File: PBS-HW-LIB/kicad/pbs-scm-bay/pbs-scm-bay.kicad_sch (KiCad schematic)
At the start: 10 parts, among them J1 Module receptacle, blind-mate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, J2 Host harness connector, J3 Identity tag pigtail connecto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, J4 Coaxial host antenna port (SC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, SW1 Module-seated switch (signal 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, U1 ESD/TVS protection array (dat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

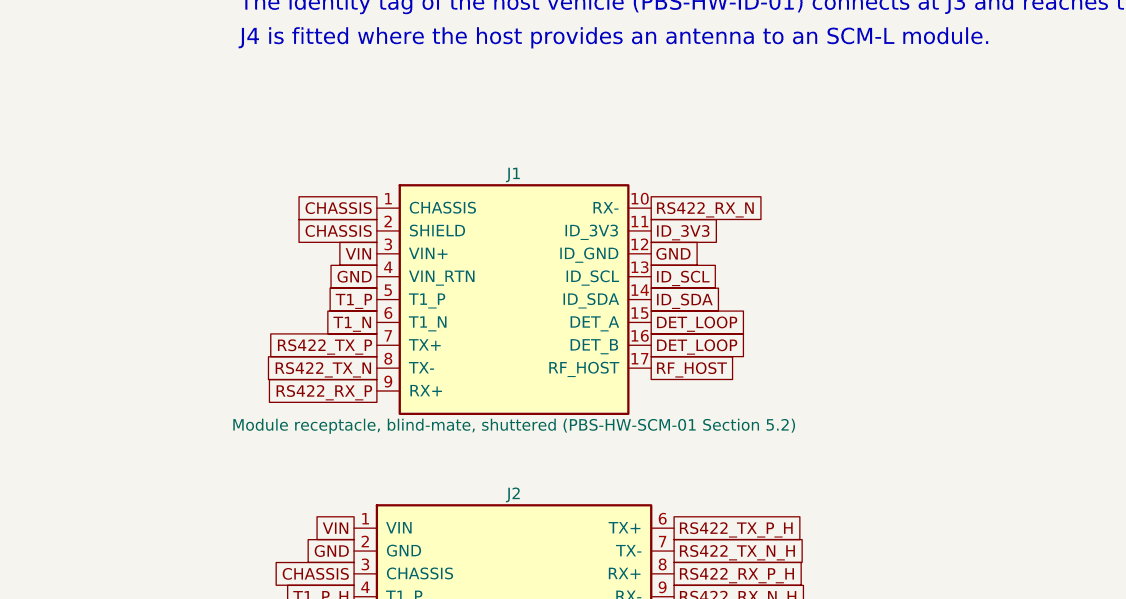
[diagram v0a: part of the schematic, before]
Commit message: Define the module host connector (PBS-HW-CON-01)
Add PBS-HW-CON-01: a face-to-face blind-mate connector with 17 contacts at
stated positions, flat pads on the module and spring contacts in the bay,
mating order set by four free heights 0.60 mm apart, keyed guide pins
(A 4.00, B 3.00), a bay cover plate and covered module apertures, an SMP
RF contact, forces and electrical ratings. Two dimensioned drawing sheets.

KiCad: both J1 footprints now follow the contact map (module half on the
back of the core board, centred; bay half with spring-contact holes and
guide pins), with 3D models showing contact heights, guide pins and the
cover plate. All geometry comes from tools/connector.py.

PBS-HW-SCM-01 v0.3 references the connector document.
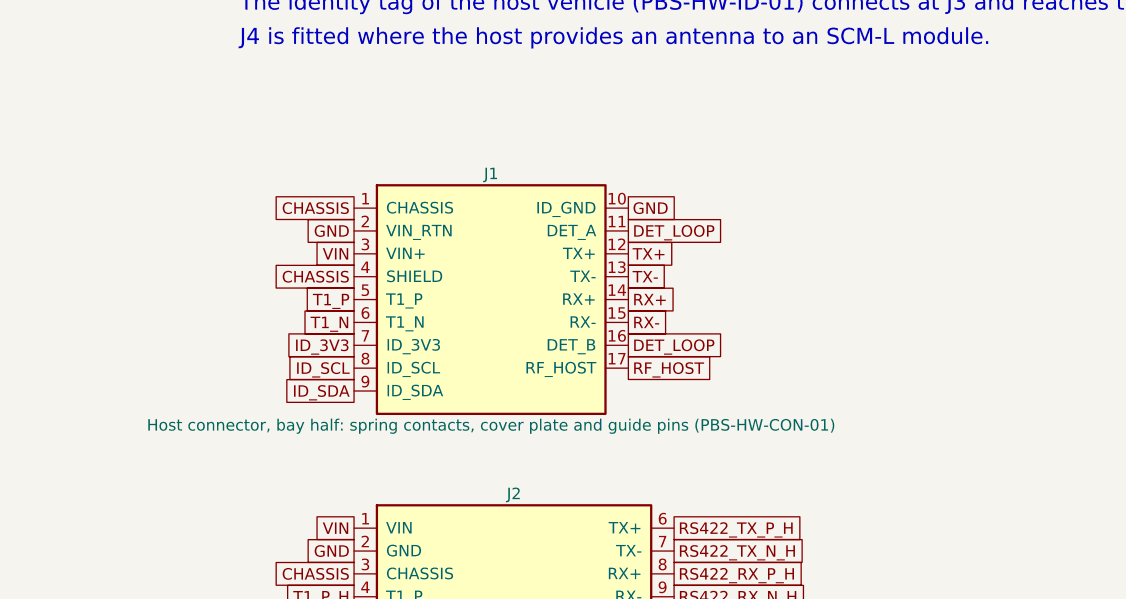
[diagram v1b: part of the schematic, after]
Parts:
- J1: value Module receptacle, blind-mate, shuttered (PBS-HW-SCM-01 Section 5.2) -> Host connector, bay half: spring contacts, cover plate and guide pins (PBS-HW-CON-01); footprint PBS_Generic:J1_Module_receptacle_blind_mate_shuttered_PBS_HW_SCM_01_Section_5_2 -> PBS_Generic:J1_Host_connector_bay_half_spring_contacts_cover_plate_and_guide_pins_PBS_HW_CON; symbol PBS_Generic:J1_Module_receptacle_blind_mate_shuttered_PBS_HW_SCM_01_Section_5_2 -> PBS_Generic:J1_Host_connector_bay_half_spring_contacts_cover_plate_and_guide_pins_PBS_HW_CON
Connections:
- net CHASSIS: now also J1.4 (SHIELD); no longer J1.2 (SHIELD)
- net DET_LOOP: now also J1.11 (DET_A); no longer J1.15 (DET_A)
- net GND: now also J1.10 (ID_GND), J1.2 (VIN_RTN); no longer J1.12 (ID_GND), J1.4 (VIN_RTN)
- net ID_3V3: now also J1.7 (ID_3V3); no longer J1.11 (ID_3V3)
- net ID_SCL: now also J1.8 (ID_SCL); no longer J1.13 (ID_SCL)
- net ID_SDA: now also J1.9 (ID_SDA); no longer J1.14 (ID_SDA)
- net RS422_RX_N: no longer J1.10 (RX-)
- net RS422_RX_P: no longer J1.9 (RX+)
- net RS422_TX_N: no longer J1.8 (TX-)
- net RS422_TX_P: no longer J1.7 (TX+)
- new net RX+: J1.14 (RX+)
- new net RX-: J1.15 (RX-)
- new net TX+: J1.12 (TX+)
- new net TX-: J1.13 (TX-)
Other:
- moved on the sheet: J1
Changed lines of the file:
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@@
 (kicad_sch (version 20231120) (generator "eeschema") (generator_version "8.0")
   (paper "A3")
-  (title_block (title "PBS-HW-SCM-01 host bay interface board: Bay interface") (date "2026-10-08") (rev "0.2") (company "Pale Blue Systems Foundation") (comment 1 "PBS-HW-SCM-01 open reference design; generic placeholders, no part numbers") (comment 2 "Generated by PBS-HW-LIB/kicad/tools/generate.py"))
-  (symbol (lib_id "PBS_Generic:J1_Module_receptacle_blind_mate_shuttered_PBS_HW_SCM_01_Section_5_2") (at 55.88 55.88 0) (unit 1) (exclude_from_sim no) (in_bom yes) (on_board yes) (dnp no)
-    (property "Reference" "J1" (at 55.88 41.91 0) (effects (font (size 1.27 1.27))))
-    (property "Value" "Module receptacle, blind-mate, shuttered (PBS-HW-SCM-01 Section 5.2)" (at 55.88 69.85 0) (effects (font (size 1.27 1.27))))
-    (property "Footprint" "PBS_Generic:J1_Module_receptacle_blind_mate_shuttered_PBS_HW_SCM_01_Section_5_2" (at 55.88 55.88 0) (effects (font (size 1.27 1.27)) hide))
-    (property "Datasheet" "" (at 55.88 55.88 0) (effects (font (size 1.27 1.27)) hide))
-    (property "Description" "Generic placeholder: Module receptacle, blind-mate, shuttered (PBS-HW-SCM-01 Section 5.2)" (at 55.88 55.88 0) (effects (font (size 1.27 1.27)) hide))
-    (property "Fit" "All" (at 55.88 72.39 0) (effects (font (size 1.27 1.27)) hide))
+  (title_block (title "PBS-HW-SCM-01 host bay interface board: Bay interface") (date "2026-10-08") (rev "0.3") (company "Pale Blue Systems Foundation") (comment 1 "PBS-HW-SCM-01 open reference design; generic placeholders, no part numbers") (comment 2 "Generated by PBS-HW-LIB/kicad/tools/generate.py"))
+  (symbol (lib_id "PBS_Generic:J1_Host_connector_bay_half_spring_contacts_cover_plate_and_guide_pins_PBS_HW_CON") (at 53.34 55.88 0) (unit 1) (exclude_from_sim no) (in_bom yes) (on_board yes) (dnp no)
+    (property "Reference" "J1" (at 53.34 41.91 0) (effects (font (size 1.27 1.27))))
+    (property "Value" "Host connector, bay half: spring contacts, cover plate and guide pins (PBS-HW-CON-01)" (at 53.34 69.85 0) (effects (font (size 1.27 1.27))))
+    (property "Footprint" "PBS_Generic:J1_Host_connector_bay_half_spring_contacts_cover_plate_and_guide_pins_PBS_HW_CON" (at 53.34 55.88 0) (effects (font (size 1.27 1.27)) hide))
+    (property "Datasheet" "" (at 53.34 55.88 0) (effects (font (size 1.27 1.27)) hide))
+    (property "Description" "Generic placeholder: Host connector, bay half: spring contacts, cover plate and guide pins (PBS-HW-CON-01)" (at 53.34 55.88 0) (effects (font (size 1.27 1.27)) hide))
+    (property "Fit" "All" (at 53.34 72.39 0) (effects (font (size 1.27 1.27)) hide))
     (pin "1")
     (pin "2")
@@
     (pin "17")
     (instances (project "pbs-scm-bay" (path "/f574994a-9591-5314-bf82-9cdc403f0860" (reference "J1") (unit 1)))))
-  (global_label "CHASSIS" (shape passive) (at 40.64 45.72 180) (fields_autoplaced yes) (effects (font (size 1.27 1.27)) (justify right)))
-  (global_label "CHASSIS" (shape passive) (at 40.64 48.26 180) (fields_autoplaced yes) (effects (font (size 1.27 1.27)) (justify right)))
-  (global_label "VIN" (shape passive) (at 40.64 50.8 180) (fields_autoplaced yes) (effects (font (size 1.27 1.27)) (justify right)))
-  (global_label "GND" (shape passive) (at 40.64 53.34 180) (fields_autoplaced yes) (effects (font (size 1.27 1.27)) (justify right)))
-  (global_label "T1_P" (shape passive) (at 40.64 55.88 180) (fields_autoplaced yes) (effects (font (size 1.27 1.27)) (justify right)))
-  (global_label "T1_N" (shape passive) (at 40.64 58.42 180) (fields_autoplaced yes) (effects (font (size 1.27 1.27)) (justify right)))
-  (global_label "RS422_TX_P" (shape passive) (at 40.64 60.96 180) (fields_autoplaced yes) (effects (font (size 1.27 1.27)) (justify right)))
-  (global_label "RS422_TX_N" (shape passive) (at 40.64 63.5 180) (fields_autoplaced yes) (effects (font (size 1.27 1.27)) (justify right)))
-  (global_label "RS422_RX_P" (shape passive) (at 40.64 66.04 180) (fields_autoplaced yes) (effects (font (size 1.27 1.27)) (justify right)))
-  (global_label "RS422_RX_N" (shape passive) (at 71.12 45.72 0) (fields_autoplaced yes) (effects (font (size 1.27 1.27)) (justify left)))
-  (global_label "ID_3V3" (shape passive) (at 71.12 48.26 0) (fields_autoplaced yes) (effects (font (size 1.27 1.27)) (justify left)))
-  (global_label "GND" (shape passive) (at 71.12 50.8 0) (fields_autoplaced yes) (effects (font (size 1.27 1.27)) (justify left)))
-  (global_label "ID_SCL" (shape passive) (at 71.12 53.34 0) (fields_autoplaced yes) (effects (font (size 1.27 1.27)) (justify left)))
-  (global_label "ID_SDA" (shape passive) (at 71.12 55.88 0) (fields_autoplaced yes) (effects (font (size 1.27 1.27)) (justify left)))
-  (global_label "DET_LOOP" (shape passive) (at 71.12 58.42 0) (fields_autoplaced yes) (effects (font (size 1.27 1.27)) (justify left)))
-  (global_label "DET_LOOP" (shape passive) (at 71.12 60.96 0) (fields_autoplaced yes) (effects (font (size 1.27 1.27)) (justify left)))
-  (global_label "RF_HOST" (shape passive) (at 71.12 63.5 0) (fields_autoplaced yes) (effects (font (size 1.27 1.27)) (justify left)))
+  (global_label "CHASSIS" (shape passive) (at 38.1 45.72 180) (fields_autoplaced yes) (effects (font (size 1.27 1.27)) (justify right)))
+  (global_label "GND" (shape passive) (at 38.1 48.26 180) (fields_autoplaced yes) (effects (font (size 1.27 1.27)) (justify right)))
+  (global_label "VIN" (shape passive) (at 38.1 50.8 180) (fields_autoplaced yes) (effects (font (size 1.27 1.27)) (justify right)))
+  (global_label "CHASSIS" (shape passive) (at 38.1 53.34 180) (fields_autoplaced yes) (effects (font (size 1.27 1.27)) (justify right)))
+  (global_label "T1_P" (shape passive) (at 38.1 55.88 180) (fields_autoplaced yes) (effects (font (size 1.27 1.27)) (justify right)))
+  (global_label "T1_N" (shape passive) (at 38.1 58.42 180) (fields_autoplaced yes) (effects (font (size 1.27 1.27)) (justify right)))
+  (global_label "ID_3V3" (shape passive) (at 38.1 60.96 180) (fields_autoplaced yes) (effects (font (size 1.27 1.27)) (justify right)))
+  (global_label "ID_SCL" (shape passive) (at 38.1 63.5 180) (fields_autoplaced yes) (effects (font (size 1.27 1.27)) (justify right)))
+  (global_label "ID_SDA" (shape passive) (at 38.1 66.04 180) (fields_autoplaced yes) (effects (font (size 1.27 1.27)) (justify right)))
+  (global_label "GND" (shape passive) (at 68.58 45.72 0) (fields_autoplaced yes) (effects (font (size 1.27 1.27)) (justify left)))
+  (global_label "DET_LOOP" (shape passive) (at 68.58 48.26 0) (fields_autoplaced yes) (effects (font (size 1.27 1.27)) (justify left)))
+  (global_label "TX+" (shape passive) (at 68.58 50.8 0) (fields_autoplaced yes) (effects (font (size 1.27 1.27)) (justify left)))
+  (global_label "TX-" (shape passive) (at 68.58 53.34 0) (fields_autoplaced yes) (effects (font (size 1.27 1.27)) (justify left)))
+  (global_label "RX+" (shape passive) (at 68.58 55.88 0) (fields_autoplaced yes) (effects (font (size 1.27 1.27)) (justify left)))
+  (global_label "RX-" (shape passive) (at 68.58 58.42 0) (fields_autoplaced yes) (effects (font (size 1.27 1.27)) (justify left)))
+  (global_label "DET_LOOP" (shape passive) (at 68.58 60.96 0) (fields_autoplaced yes) (effects (font (size 1.27 1.27)) (justify left)))
+  (global_label "RF_HOST" (shape passive) (at 68.58 63.5 0) (fields_autoplaced yes) (effects (font (size 1.27 1.27)) (justify left)))
   (symbol (lib_id "PBS_Generic:J2_Host_harness_connector") (at 55.88 86.36 0) (unit 1) (exclude_from_sim no) (in_bom yes) (on_board yes) (dnp no)
     (property "Reference" "J2" (at 55.88 77.47 0) (effects (font (size 1.27 1.27))))
